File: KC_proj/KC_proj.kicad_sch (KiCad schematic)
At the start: 2 parts, among them U1 STM32C011F6Px, U2 MAX-M10S

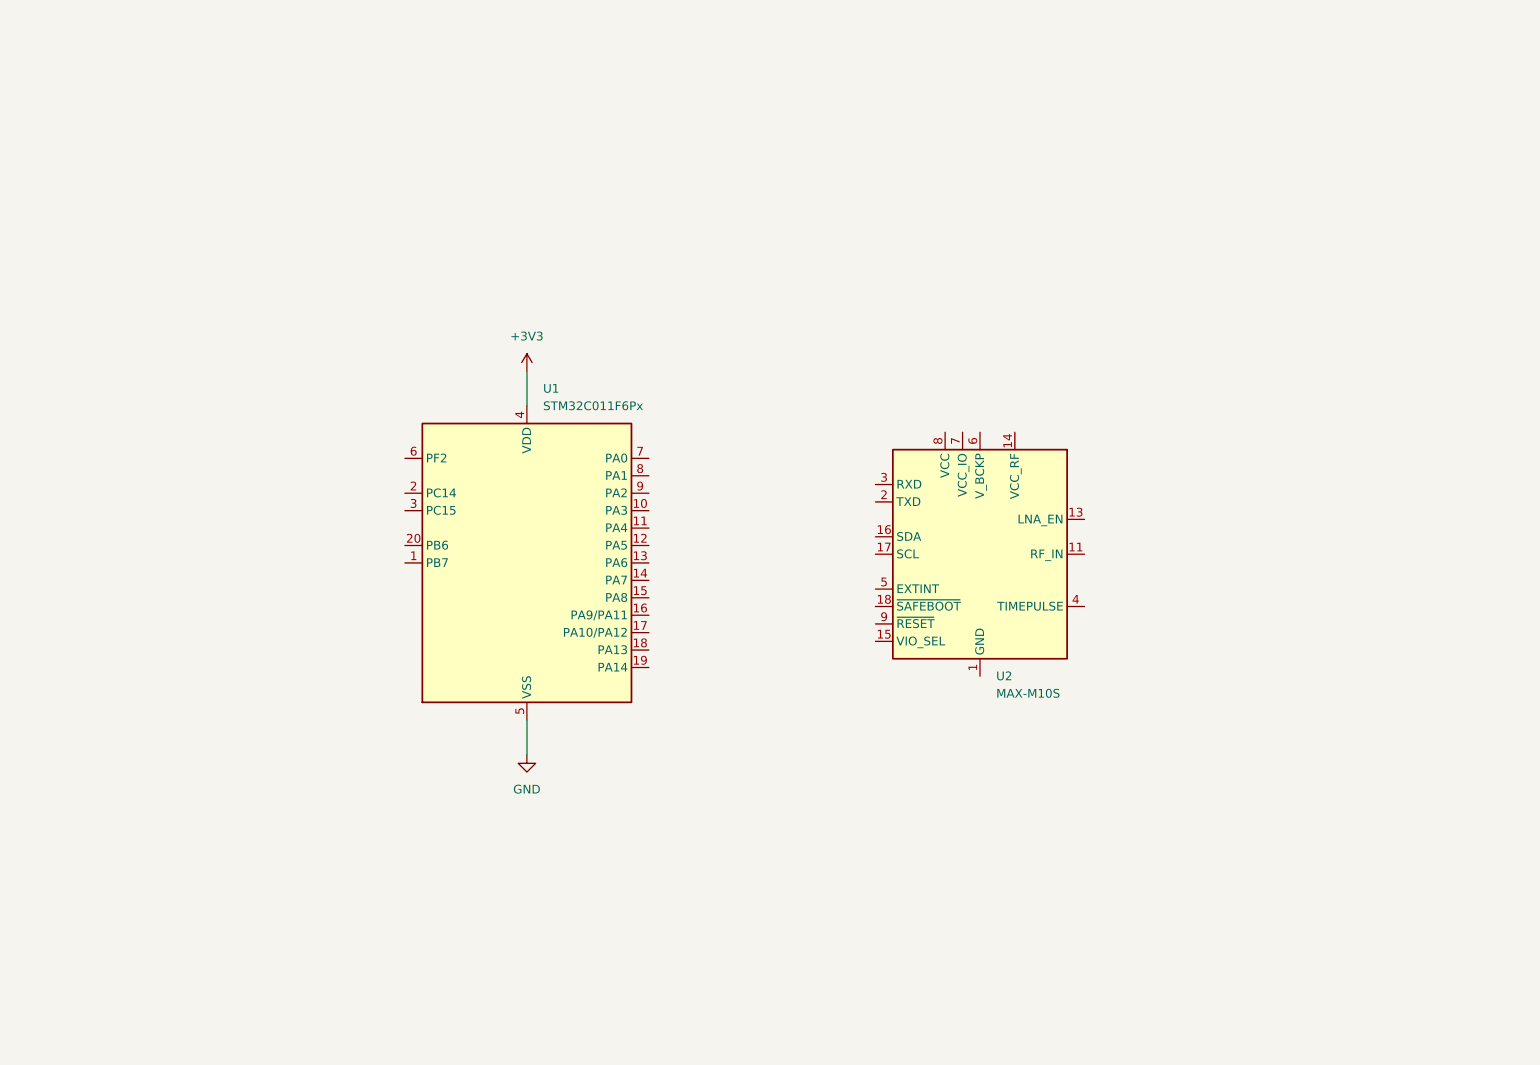
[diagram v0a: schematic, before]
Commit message: wire kicad diags
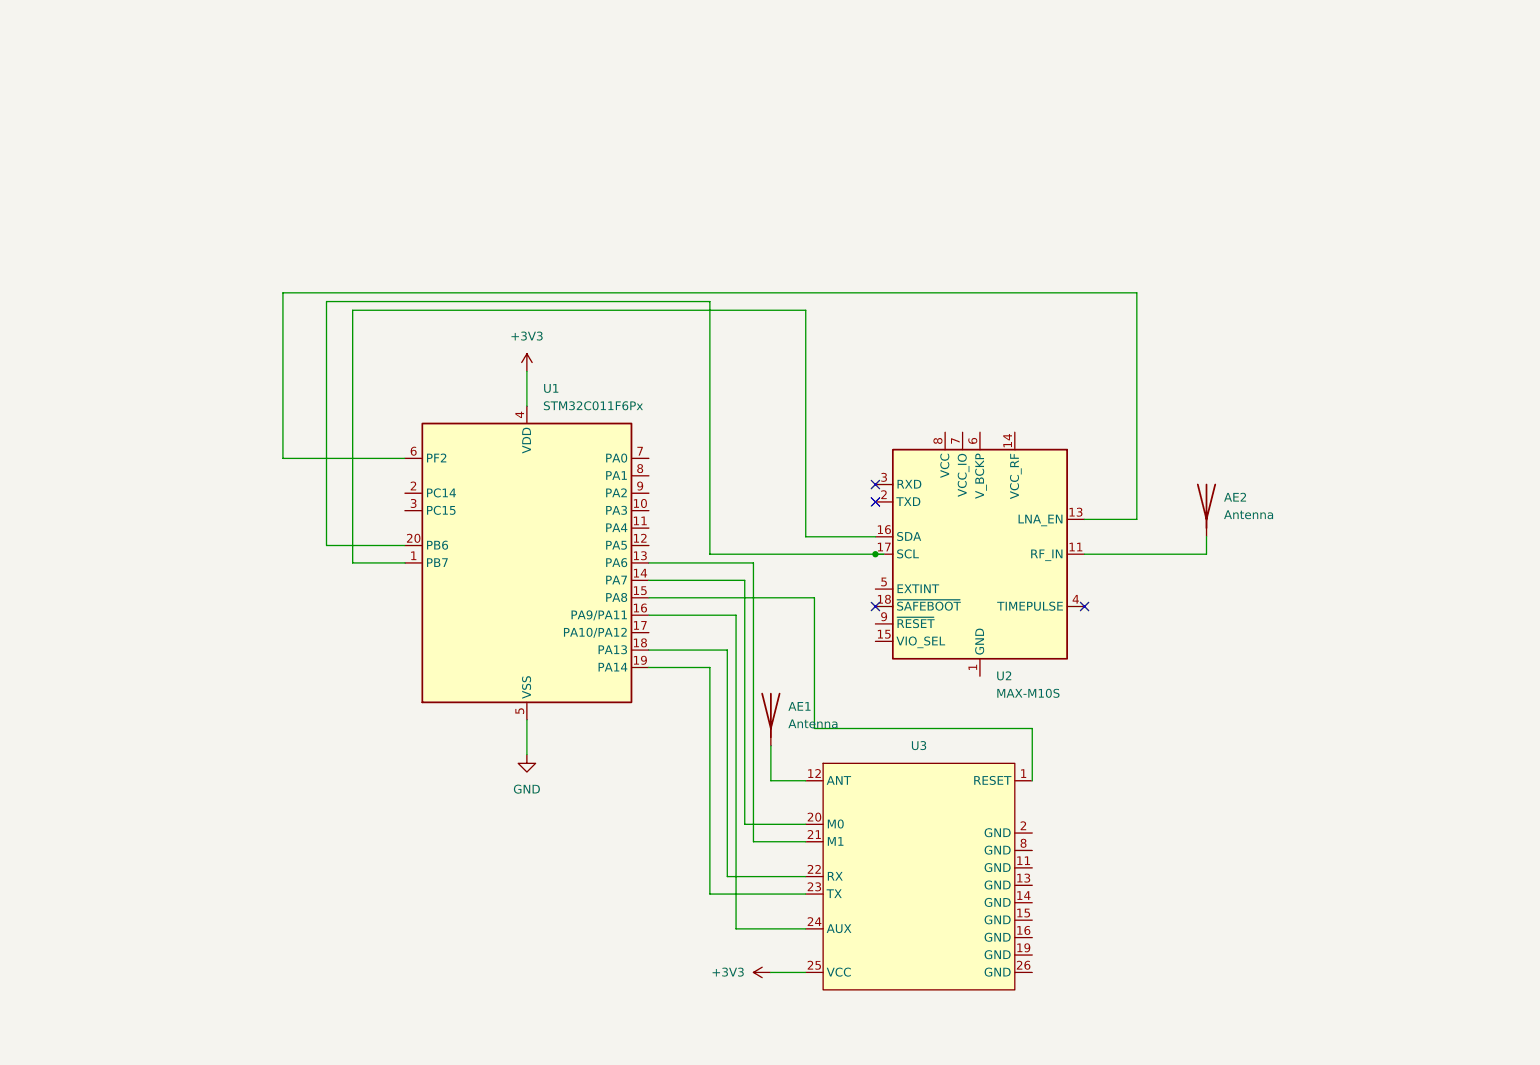
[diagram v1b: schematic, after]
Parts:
- added AE1, AE2: Antenna, symbol Device:Antenna
- added U3: (no value), symbol E22-900T22S:E22-900T22S
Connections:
- net +3V3: now also U3.25 (VCC)
- net at U2.11 (RF_IN): now also AE2.1 (A)
- net at U2.13 (LNA_EN): now also U1.6 (PF2)
- net at U2.16 (SDA): now also U1.1 (PB7)
- net at U2.17 (SCL): now also U1.20 (PB6)
- net at U1.13 (PA6): now also U3.21 (M1)
- net at U1.14 (PA7): now also U3.20 (M0)
- net at U1.15 (PA8): now also U3.1 (RESET)
- net at U1.16 (PA9/PA11): now also U3.24 (AUX)
- net at U1.18 (PA13): now also U3.22 (RX)
- net at U1.19 (PA14): now also U3.23 (TX)
- new net: AE1.1 (A), U3.12 (ANT)
- no-connect marks 0 -> 4

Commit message: Remake Cmake project with new MCU. Finish PCB Design v1 for review.
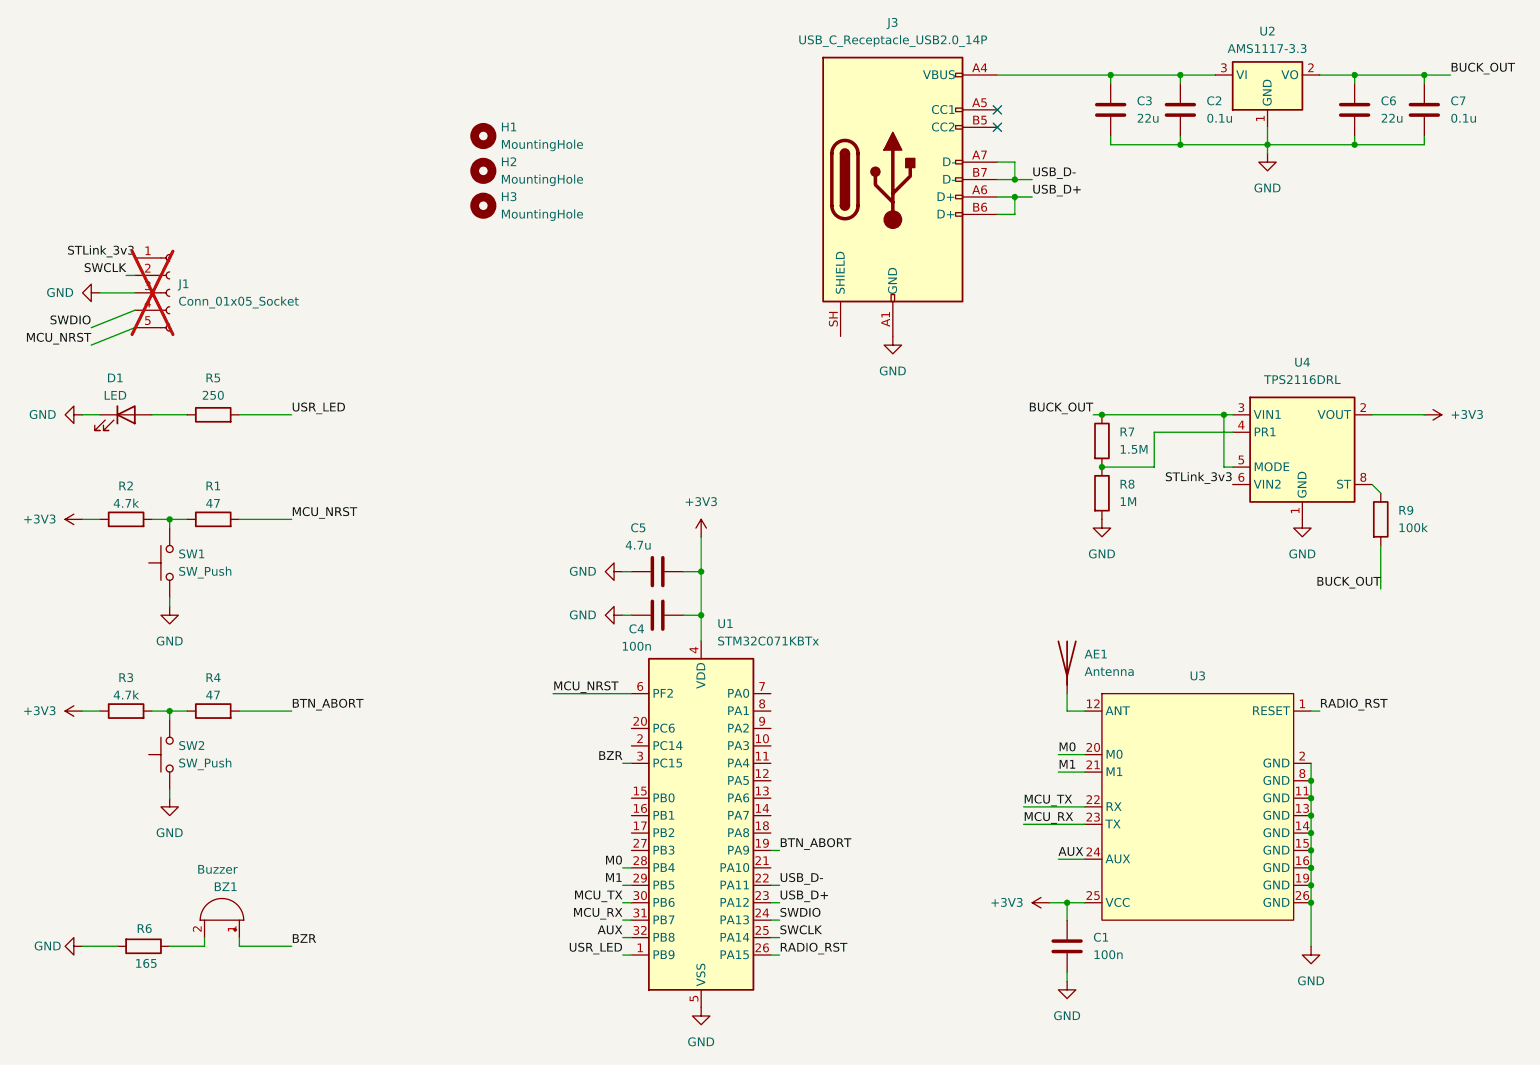
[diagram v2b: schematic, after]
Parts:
- removed AE2: Antenna, symbol Device:Antenna
- removed U1: STM32C011F6Px, Package_SO:TSSOP-20_4.4x6.5mm_P0.65mm, symbol MCU_ST_STM32C0:STM32C011F6Px
- removed U2: MAX-M10S, RF_GPS:ublox_MAX, symbol RF_GPS:MAX-M10S
- added BZ1: Buzzer, Buzzer_Beeper:Buzzer_12x9.5RM7.6, symbol Device:Buzzer
- added C1, C4: 100n, Capacitor_SMD:C_0603_1608Metric, symbol Device:C
- added C2, C7: 0.1u, Capacitor_SMD:C_0603_1608Metric, symbol Device:C
- added C3, C6: 22u, Capacitor_SMD:C_0603_1608Metric, symbol Device:C
- added C5: 4.7u, Capacitor_SMD:C_0603_1608Metric, symbol Device:C
- added D1: LED, LED_SMD:LED_1206_3216Metric, symbol Device:LED
- added H1, H2, H3: MountingHole, MountingHole:MountingHole_2.2mm_M2, symbol Mechanical:MountingHole
- added J1: Conn_01x05_Socket, Connector_PinHeader_2.54mm:PinHeader_1x05_P2.54mm_Vertical, symbol Connector:Conn_01x05_Socket
- added J3: USB_C_Receptacle_USB2.0_14P, Connector_USB:USB_C_Receptacle_HRO_TYPE-C-31-M-12, symbol Connector:USB_C_Receptacle_USB2.0_14P
- added R1, R4: 47, Resistor_SMD:R_0603_1608Metric, symbol Device:R
- added R2, R3: 4.7k, Resistor_SMD:R_0603_1608Metric, symbol Device:R
- added R5: 250, Resistor_SMD:R_0603_1608Metric, symbol Device:R
- added R6: 165, Resistor_SMD:R_0603_1608Metric, symbol Device:R
- added R7: 1.5M, Resistor_SMD:R_0603_1608Metric, symbol Device:R
- added R8: 1M, Resistor_SMD:R_0603_1608Metric, symbol Device:R
- added R9: 100k, Resistor_SMD:R_0603_1608Metric, symbol Device:R
- added SW1, SW2: SW_Push, Button_Switch_SMD:SW_Push_1P1T_NO_CK_KSC6xxJ, symbol Switch:SW_Push
- added U1: STM32C071KBTx, Package_QFP:LQFP-32_7x7mm_P0.8mm, symbol MCU_ST_STM32C0:STM32C071KBTx
- added U2: AMS1117-3.3, Package_TO_SOT_SMD:SOT-223-3_TabPin2, symbol Regulator_Linear:AMS1117-3.3
- added U4: TPS2116DRL, Package_TO_SOT_SMD:SOT-583-8, symbol Power_Management:TPS2116DRL
- AE1: footprint (none) -> Connector_Coaxial:SMA_Amphenol_901-143_Horizontal
- U3: footprint (none) -> KC_proj:E22-900T22S
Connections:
- net +3V3: now also C1.1, C4.2, C5.2, R2.1, R3.1, U1.4 (VDD), U4.2 (VOUT), U4.7 (VOUT)
- net GND: now also U3.11 (GND), U3.13 (GND), U3.14 (GND), U3.15 (GND), U3.16 (GND), U3.19 (GND), U3.2 (GND), U3.26 (GND), U3.8 (GND), C1.2, C2.2, C3.2, C4.1, C5.1, C6.2, C7.2, D1.1 (K), J1.3 (Pin_3), J3.A1 (GND), J3.A12 (GND), J3.B1 (GND), J3.B12 (GND), R6.2, R8.2, SW1.1, SW2.1, U1.5 (VSS), U2.1 (GND), U4.1 (GND)
- net RADIO_RST: now reaches U3.1 (RESET)
- net RADIO_RST: now also U1.26 (PA15)
- net M0: now reaches U3.20 (M0)
- net M0: now also U1.28 (PB4)
- net M1: now reaches U3.21 (M1)
- net M1: now also U1.29 (PB5)
- net MCU_TX: now reaches U3.22 (RX)
- net MCU_TX: now also U1.30 (PB6)
- net MCU_RX: now reaches U3.23 (TX)
- net MCU_RX: now also U1.31 (PB7)
- net AUX: now reaches U3.24 (AUX)
- net AUX: now also U1.32 (PB8)
- new net: R7.2, R8.1, U4.4 (PR1)
- new net: C2.1, C3.1, J3.A4 (VBUS), J3.A9 (VBUS), J3.B4 (VBUS), J3.B9 (VBUS), U2.3 (VI)
- new net: R3.2, R4.1, SW2.2
- new net: BZ1.2 (-), R6.1
- new net: R9.1, U4.8 (ST)
- new net: D1.2 (A), R5.1
- new net: R1.1, R2.2, SW1.2
- new net BTN_ABORT: R4.2, U1.19 (PA9)
- new net BUCK_OUT: C6.1, C7.1, R7.1, R9.2, U2.2 (VO), U4.3 (VIN1), U4.5 (MODE)
- new net BZR: BZ1.1 (+), U1.3 (PC15)
- new net MCU_NRST: J1.5 (Pin_5), R1.2, U1.6 (PF2)
- new net STLink_3v3: J1.1 (Pin_1), U4.6 (VIN2)
- new net SWCLK: J1.2 (Pin_2), U1.25 (PA14)
- new net SWDIO: J1.4 (Pin_4), U1.24 (PA13)
- new net USB_D+: J3.A6 (D+), J3.B6 (D+), U1.23 (PA12)
- new net USB_D-: J3.A7 (D-), J3.B7 (D-), U1.22 (PA11)
- new net USR_LED: R5.2, U1.1 (PB9)
- no-connect marks 4 -> 2
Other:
- moved on the sheet: AE1, U3
